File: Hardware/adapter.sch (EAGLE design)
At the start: 7 parts

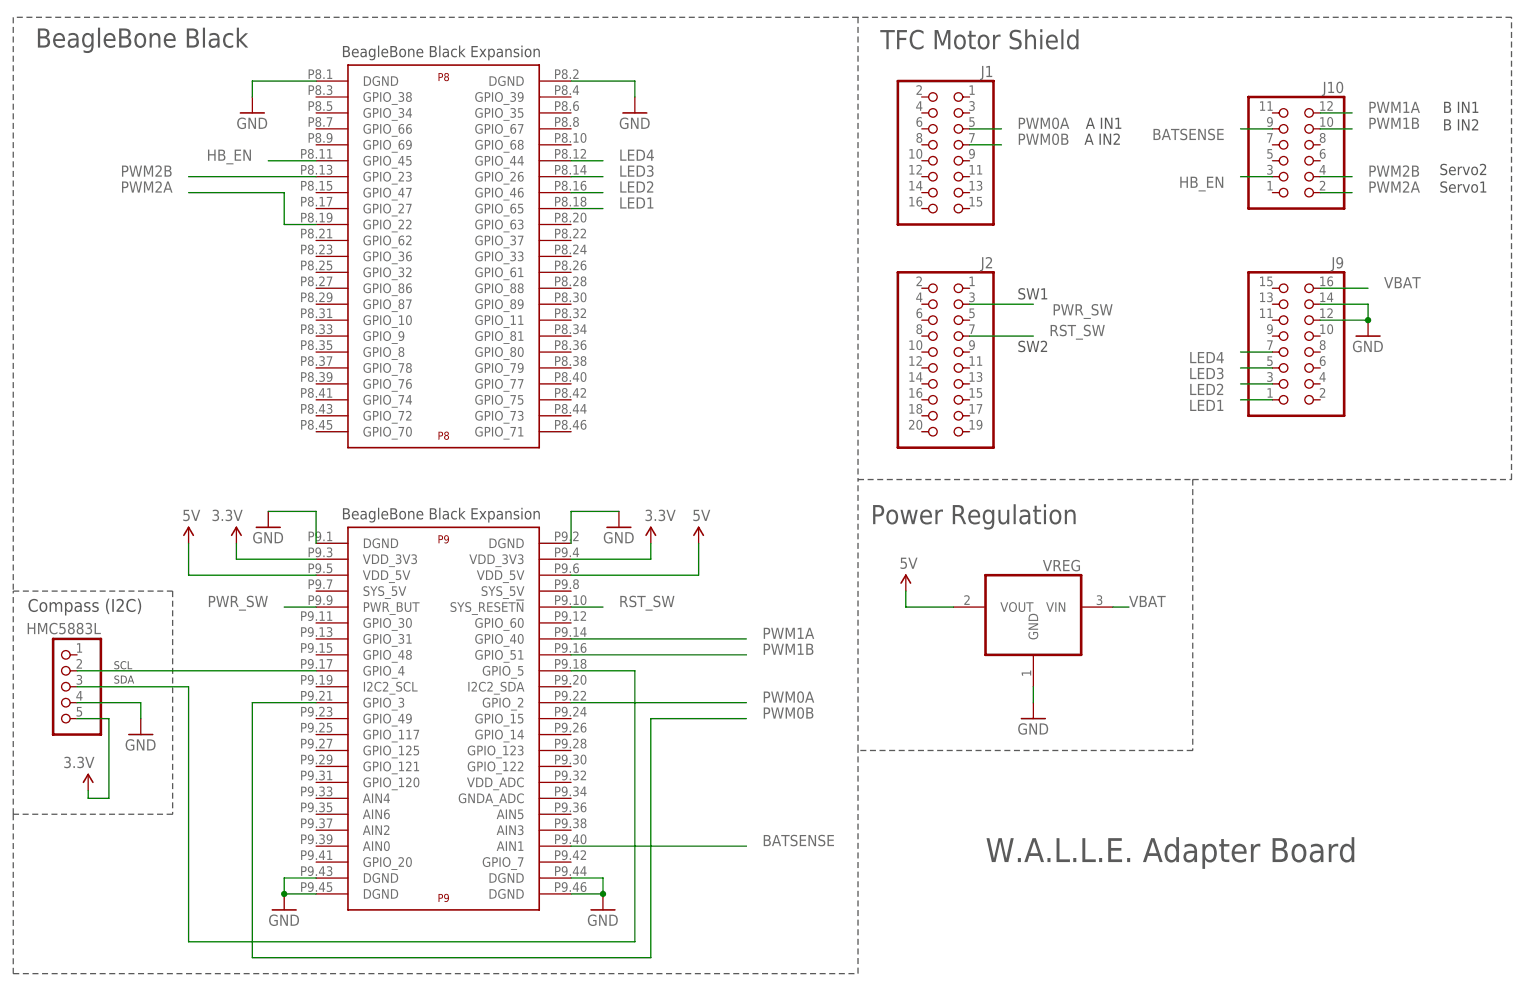
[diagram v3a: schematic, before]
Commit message: Updated header dimensions. Added Extra connector for GPIO.
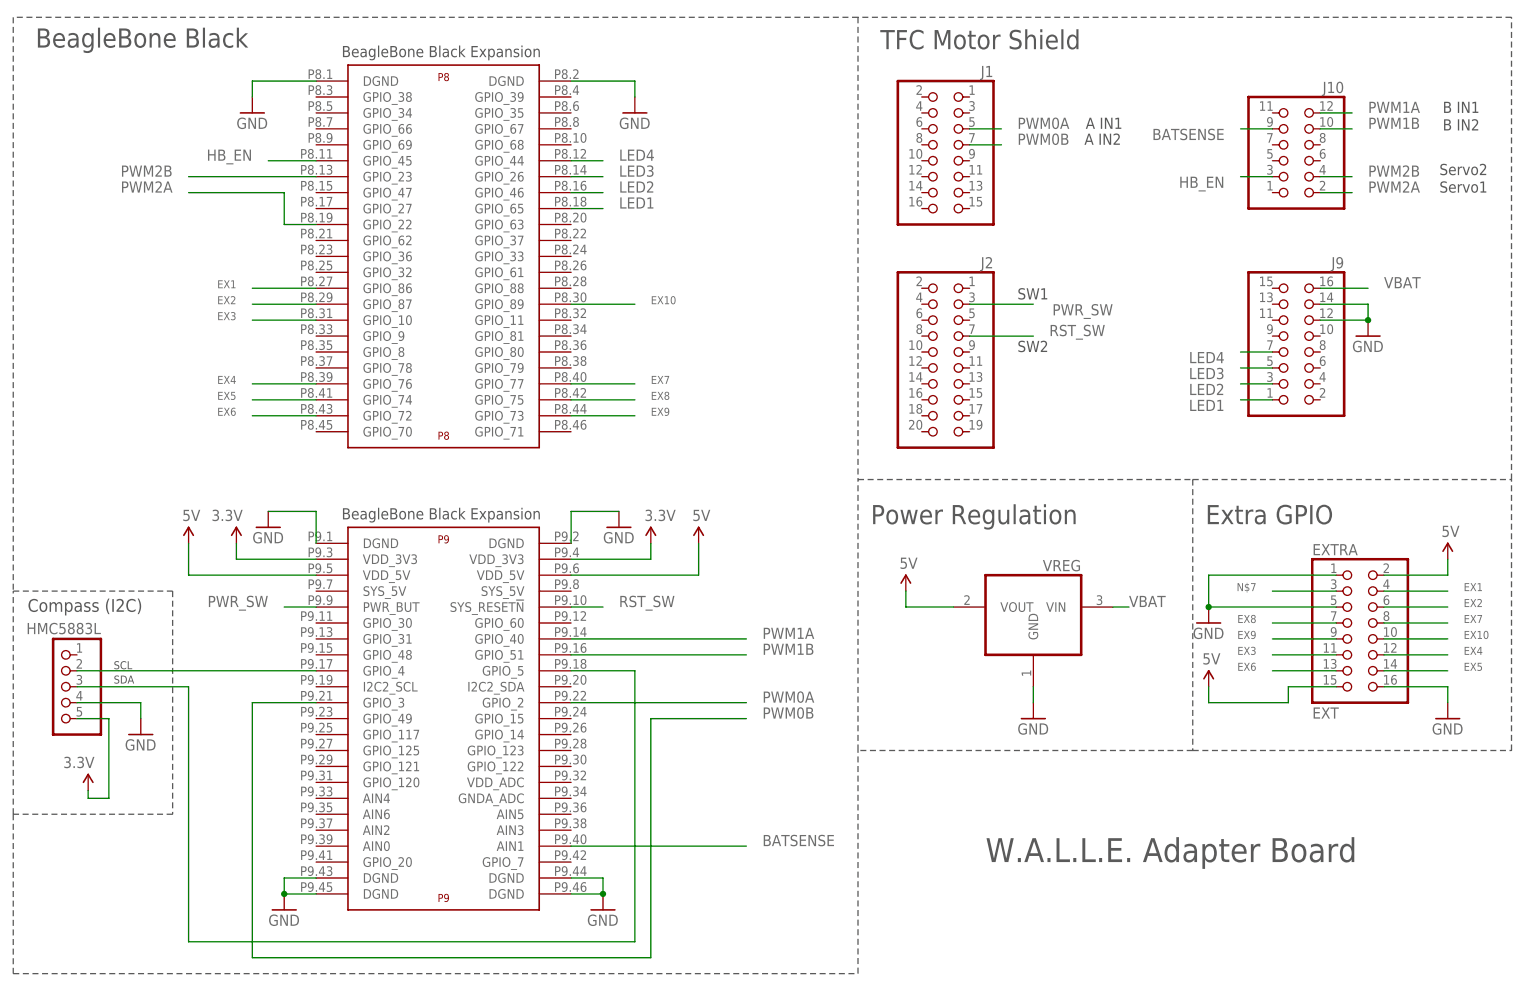
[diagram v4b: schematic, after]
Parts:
- added EXTRA: EXT, pinhead:PINHD-2X8
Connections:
- new net EX1: EXTRA.4, U$1P8.GPIO_86
- new net EX10: EXTRA.10, U$1P8.GPIO_89
- new net EX2: EXTRA.6, U$1P8.GPIO_87
- new net EX3: EXTRA.11, U$1P8.GPIO_10
- new net EX4: EXTRA.12, U$1P8.GPIO_76
- new net EX5: EXTRA.14, U$1P8.GPIO_74
- new net EX6: EXTRA.13, U$1P8.GPIO_72
- new net EX7: EXTRA.8, U$1P8.GPIO_77
- new net EX8: EXTRA.7, U$1P8.GPIO_75
- new net EX9: EXTRA.9, U$1P8.GPIO_73
- new net N$7: EXTRA.3
- net 5V: now also EXTRA.15, EXTRA.2
- net GND: now also EXTRA.1, EXTRA.16, EXTRA.5
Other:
- note added: "Extra GPIO"
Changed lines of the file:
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@@
 <part name="SUPPLY6" library="SparkFun-Aesthetics" deviceset="3.3V" device=""/>
 <part name="SUPPLY7" library="SparkFun-Aesthetics" deviceset="5V" device=""/>
+<part name="EXTRA" library="pinhead" deviceset="PINHD-2X8" device="" value="EXT"/>
+<part name="SUPPLY1" library="SparkFun-Aesthetics" deviceset="5V" device=""/>
+<part name="GND10" library="supply1" deviceset="GND" device=""/>
+<part name="GND11" library="supply1" deviceset="GND" device=""/>
+<part name="SUPPLY8" library="SparkFun-Aesthetics" deviceset="5V" device=""/>
 </parts>
 <sheets>
@@
 <text x="-34.798" y="25.908" size="1.27" layer="97">SDA</text>
 <text x="-34.798" y="28.194" size="1.27" layer="97">SCL</text>
+<wire x1="137.16" y1="15.24" x2="187.96" y2="15.24" width="0.1524" layer="97" style="shortdash"/>
+<wire x1="187.96" y1="15.24" x2="187.96" y2="58.42" width="0.1524" layer="97" style="shortdash"/>
+<text x="139.192" y="51.308" size="3.048" layer="97">Extra GPIO</text>
 </plain>
 <instances>
@@
 <instance part="SUPPLY6" gate="G$1" x="50.8" y="48.26"/>
 <instance part="SUPPLY7" gate="G$1" x="91.44" y="40.64"/>
+<instance part="EXTRA" gate="A" x="162.56" y="35.56"/>
+<instance part="SUPPLY1" gate="G$1" x="177.8" y="45.72"/>
+<instance part="GND10" gate="1" x="139.7" y="35.56"/>
+<instance part="GND11" gate="1" x="177.8" y="20.32"/>
+<instance part="SUPPLY8" gate="G$1" x="139.7" y="25.4"/>
 </instances>
 <busses>
@@
 <junction x="165.1" y="83.82"/>
 </segment>
+<segment>
+<pinref part="EXTRA" gate="A" pin="1"/>
+<wire x1="160.02" y1="43.18" x2="139.7" y2="43.18" width="0.1524" layer="91"/>
+<pinref part="EXTRA" gate="A" pin="5"/>
+<wire x1="160.02" y1="38.1" x2="139.7" y2="38.1" width="0.1524" layer="91"/>
+<wire x1="139.7" y1="38.1" x2="139.7" y2="43.18" width="0.1524" layer="91"/>
+<pinref part="GND10" gate="1" pin="GND"/>
+<junction x="139.7" y="38.1"/>
+</segment>
+<segment>
+<pinref part="EXTRA" gate="A" pin="16"/>
+<wire x1="167.64" y1="25.4" x2="177.8" y2="25.4" width="0.1524" layer="91"/>
+<wire x1="177.8" y1="25.4" x2="177.8" y2="22.86" width="0.1524" layer="91"/>
+<pinref part="GND11" gate="1" pin="GND"/>
+</segment>
 </net>
 <net name="I2C1_SCL" class="0">
@@
 <pinref part="SUPPLY2" gate="G$1" pin="5V"/>
 </segment>
-</net>
+<segment>
+<pinref part="EXTRA" gate="A" pin="2"/>
+<pinref part="SUPPLY1" gate="G$1" pin="5V"/>
+<wire x1="167.64" y1="43.18" x2="177.8" y2="43.18" width="0.1524" layer="91"/>
+<wire x1="177.8" y1="43.18" x2="177.8" y2="45.72" width="0.1524" layer="91"/>
+</segment>
+<segment>
+<pinref part="EXTRA" gate="A" pin="15"/>
+<wire x1="160.02" y1="25.4" x2="152.4" y2="25.4" width="0.1524" layer="91"/>
+<wire x1="152.4" y1="25.4" x2="152.4" y2="22.86" width="0.1524" layer="91"/>
+<pinref part="SUPPLY8" gate="G$1" pin="5V"/>
+<wire x1="152.4" y1="22.86" x2="139.7" y2="22.86" width="0.1524" layer="91"/>
+<wire x1="139.7" y1="22.86" x2="139.7" y2="25.4" width="0.1524" layer="91"/>
+</segment>
+</net>
+<net name="EX6" class="0">
+<segment>
+<pinref part="U$1" gate="P8" pin="GPIO_72"/>
+<wire x1="-2.54" y1="68.58" x2="-12.7" y2="68.58" width="0.1524" layer="91"/>
+<label x="-15.24" y="68.58" size="1.27" layer="95" rot="MR0"/>
+</segment>
+<segment>
+<pinref part="EXTRA" gate="A" pin="13"/>
+<wire x1="160.02" y1="27.94" x2="149.86" y2="27.94" width="0.1524" layer="91"/>
+<label x="147.32" y="27.94" size="1.27" layer="95" rot="MR0"/>
+</segment>
+</net>
+<net name="EX5" class="0">
+<segment>
+<pinref part="U$1" gate="P8" pin="GPIO_74"/>
+<wire x1="-2.54" y1="71.12" x2="-12.7" y2="71.12" width="0.1524" layer="91"/>
+<label x="-15.24" y="71.12" size="1.27" layer="95" rot="MR0"/>
+</segment>
+<segment>
+<pinref part="EXTRA" gate="A" pin="14"/>
+<wire x1="167.64" y1="27.94" x2="177.8" y2="27.94" width="0.1524" layer="91"/>
+<label x="180.34" y="27.94" size="1.27" layer="95"/>
+</segment>
+</net>
+<net name="EX4" class="0">
+<segment>
+<pinref part="U$1" gate="P8" pin="GPIO_76"/>
+<wire x1="-2.54" y1="73.66" x2="-12.7" y2="73.66" width="0.1524" layer="91"/>
+<label x="-15.24" y="73.66" size="1.27" layer="95" rot="MR0"/>
+</segment>
+<segment>
+<pinref part="EXTRA" gate="A" pin="12"/>
+<wire x1="167.64" y1="30.48" x2="177.8" y2="30.48" width="0.1524" layer="91"/>
+<label x="180.34" y="30.48" size="1.27" layer="95"/>
+</segment>
+</net>
+<net name="EX3" class="0">
+<segment>
+<pinref part="U$1" gate="P8" pin="GPIO_10"/>
+<wire x1="-2.54" y1="83.82" x2="-12.7" y2="83.82" width="0.1524" layer="91"/>
+<label x="-15.24" y="83.82" size="1.27" layer="95" rot="MR0"/>
+</segment>
+<segment>
+<pinref part="EXTRA" gate="A" pin="11"/>
+<wire x1="160.02" y1="30.48" x2="149.86" y2="30.48" width="0.1524" layer="91"/>
+<label x="147.32" y="30.48" size="1.27" layer="95" rot="MR0"/>
+</segment>
+</net>
+<net name="EX2" class="0">
+<segment>
+<pinref part="U$1" gate="P8" pin="GPIO_87"/>
+<wire x1="-2.54" y1="86.36" x2="-12.7" y2="86.36" width="0.1524" layer="91"/>
+<label x="-15.24" y="86.36" size="1.27" layer="95" rot="MR0"/>
+</segment>
+<segment>
+<pinref part="EXTRA" gate="A" pin="6"/>
+<wire x1="167.64" y1="38.1" x2="177.8" y2="38.1" width="0.1524" layer="91"/>
+<label x="180.34" y="38.1" size="1.27" layer="95"/>
+</segment>
+</net>
+<net name="EX1" class="0">
+<segment>
+<pinref part="U$1" gate="P8" pin="GPIO_86"/>
+<wire x1="-2.54" y1="88.9" x2="-12.7" y2="88.9" width="0.1524" layer="91"/>
+<label x="-15.24" y="88.9" size="1.27" layer="95" rot="MR0"/>
+</segment>
+<segment>
+<pinref part="EXTRA" gate="A" pin="4"/>
+<wire x1="167.64" y1="40.64" x2="177.8" y2="40.64" width="0.1524" layer="91"/>
+<label x="180.34" y="40.64" size="1.27" layer="95"/>
+</segment>
+</net>
+<net name="N$7" class="0">
+<segment>
+<pinref part="EXTRA" gate="A" pin="3"/>
+<wire x1="160.02" y1="40.64" x2="149.86" y2="40.64" width="0.1524" layer="91"/>
+<label x="147.32" y="40.64" size="1.27" layer="95" rot="MR0"/>
+</segment>
+</net>
+<net name="EX9" class="0">
+<segment>
+<pinref part="U$1" gate="P8" pin="GPIO_73"/>
+<wire x1="38.1" y1="68.58" x2="48.26" y2="68.58" width="0.1524" layer="91"/>
+<label x="50.8" y="68.58" size="1.27" layer="95"/>
+</segment>
+<segment>
+<pinref part="EXTRA" gate="A" pin="9"/>
+<wire x1="160.02" y1="33.02" x2="149.86" y2="33.02" width="0.1524" layer="91"/>
+<label x="147.32" y="33.02" size="1.27" layer="95" rot="MR0"/>
+</segment>
+</net>
+<net name="EX8" class="0">
+<segment>
+<pinref part="U$1" gate="P8" pin="GPIO_75"/>
+<wire x1="38.1" y1="71.12" x2="48.26" y2="71.12" width="0.1524" layer="91"/>
+<label x="50.8" y="71.12" size="1.27" layer="95"/>
+</segment>
+<segment>
+<pinref part="EXTRA" gate="A" pin="7"/>
+<wire x1="160.02" y1="35.56" x2="149.86" y2="35.56" width="0.1524" layer="91"/>
+<label x="147.32" y="35.56" size="1.27" layer="95" rot="MR0"/>
+</segment>
+</net>
+<net name="EX7" class="0">
+<segment>
+<pinref part="U$1" gate="P8" pin="GPIO_77"/>
+<wire x1="38.1" y1="73.66" x2="48.26" y2="73.66" width="0.1524" layer="91"/>
+<label x="50.8" y="73.66" size="1.27" layer="95"/>
+</segment>
+<segment>
+<pinref part="EXTRA" gate="A" pin="8"/>
+<wire x1="167.64" y1="35.56" x2="177.8" y2="35.56" width="0.1524" layer="91"/>
+<label x="180.34" y="35.56" size="1.27" layer="95"/>
+</segment>
+</net>
+<net name="EX10" class="0">
+<segment>
+<pinref part="U$1" gate="P8" pin="GPIO_89"/>
+<wire x1="38.1" y1="86.36" x2="48.26" y2="86.36" width="0.1524" layer="91"/>
+<label x="50.8" y="86.36" size="1.27" layer="95"/>
+</segment>
+<segment>
+<pinref part="EXTRA" gate="A" pin="10"/>
+<wire x1="167.64" y1="33.02" x2="177.8" y2="33.02" width="0.1524" layer="91"/>
+<label x="180.34" y="33.02" size="1.27" layer="95"/>
+</segment>
+</net>
